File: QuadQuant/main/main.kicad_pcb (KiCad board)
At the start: 2 copper layers, 30.5 x 101.6 mm, 71 parts, among them J1 USB_B_Mini, J10 CV4, J11 Trig1, J12 Trig2, J13 Trig4, J14 Trig3, J2 Conn_02x05_Odd_Even, J3 OUT2, J4 OUT3, J5 OUT4, J6 OUT1, J7 CV1, J8 CV2, J9 CV3, Q1 MMBT3904, Q2 MMBT3904, Q3 MMBT3904, Q4 MMBT3904, U1 LM7805_TO220, U2 ATmega32U4-AU, U3 MCP4728, U4 TL074, Y1 Crystal16mhz

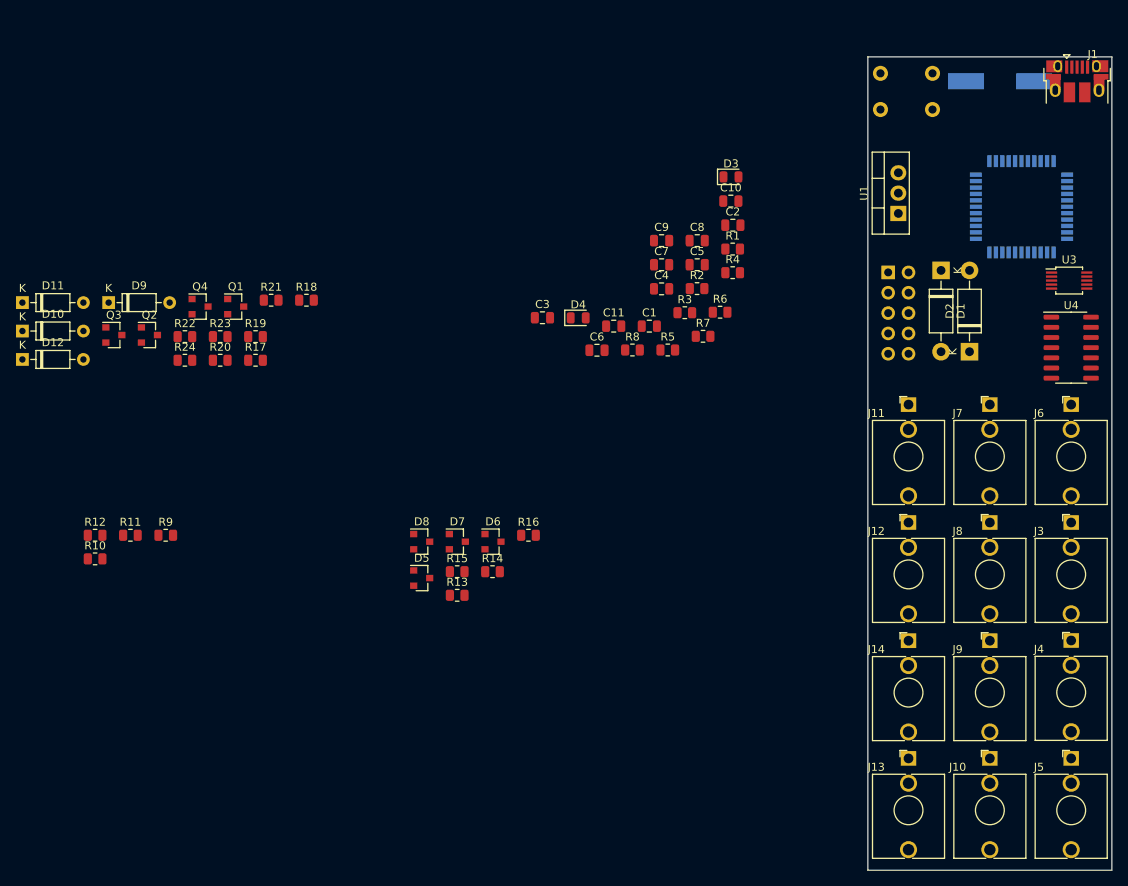
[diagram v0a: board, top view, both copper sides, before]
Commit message: Adding programming headers
Also starting in on a PCB layout. My smd work is so fugly right now.
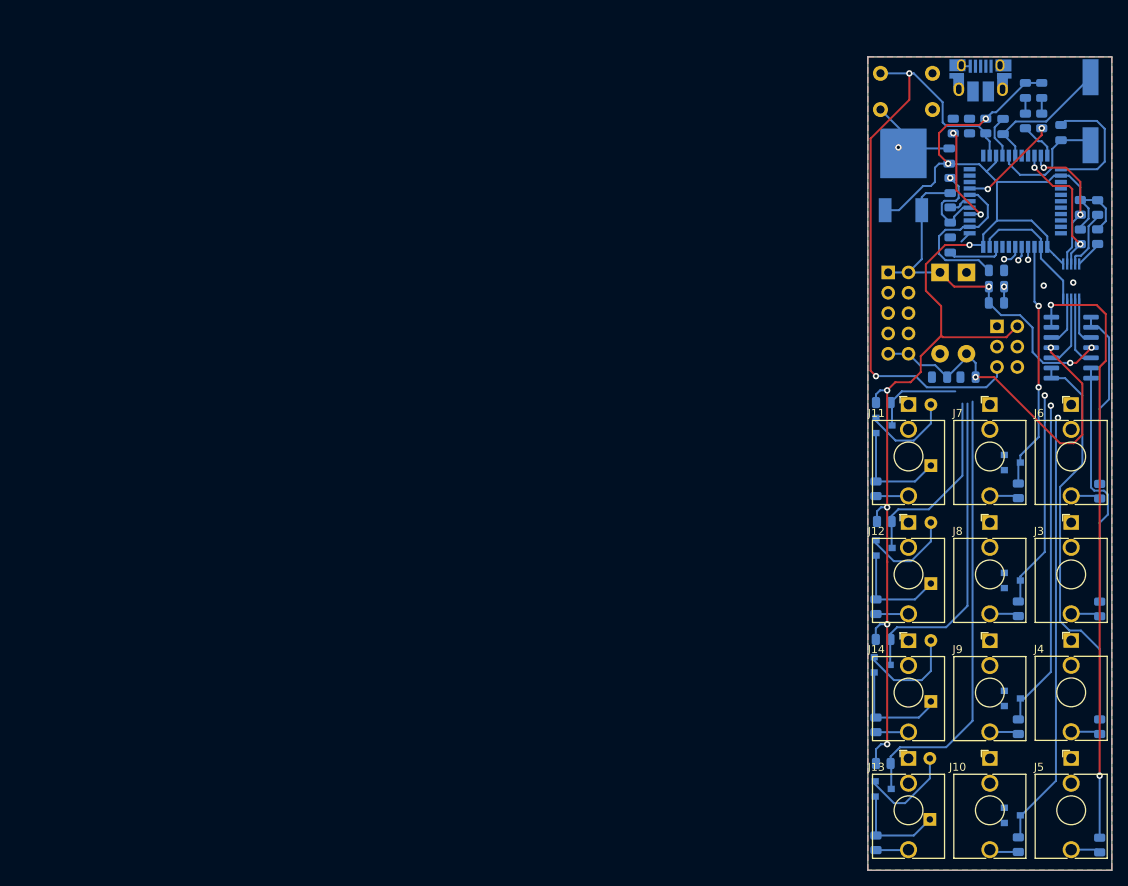
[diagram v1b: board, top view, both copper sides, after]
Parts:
- removed U1: LM7805_TO220, Package_TO_SOT_THT:TO-220-3_Vertical
- added IC1: MC7805CDTRKG, SamacSys_Parts:MJD1221G, B.Cu at (156.8, 68.5)
- added J15: Conn_02x03_Odd_Even, Connector_PinSocket_2.54mm:PinSocket_2x03_P2.54mm_Vertical, B.Cu at (168.5, 84.5)
- added R25: 1K, Resistor_SMD:R_0805_2012Metric, B.Cu at (172.1, 58.8)
- C1, C10, C11, C2, C3, C4, C5, C6, C7, C8, C9, D1, D10, D11, D12, D2, D3, D4, D5, D6, D7, D8, D9, J1, Q1, Q2, Q3, Q4, R1, R10, R11, R12, R13, R14, R15, R16, R17, R18, R19, R2, R20, R21, R22, R23, R24, R3, R4, R5, R6, R7, R8, R9, U3, U4: moved to B.Cu
- moved D11 130.4 mm to (160.1, 146.1), turned to 90 degrees
- moved R10 127.2 mm to (181.4, 134.5), turned to 90 degrees
- moved R11 127.1 mm to (181.4, 149.2), turned to 90 degrees
- moved R12 125.6 mm to (181.4, 105.1), turned to 90 degrees
- moved D12 121.3 mm to (160.3, 131.3), turned to 90 degrees
- moved D10 117.8 mm to (160.3, 116.6), turned to 90 degrees
- moved R9 117.0 mm to (181.4, 119.8), turned to 90 degrees
- moved Q3 111.6 mm to (154.3, 142.2)
- moved D9 104.7 mm to (160.3, 101.9), turned to 90 degrees
- moved R21 101.5 mm to (153.4, 149.0), turned to 270 degrees
- moved R22 99.0 mm to (153.4, 134.2), turned to 270 degrees
- moved R23 98.5 mm to (154.3, 139.1), turned to 180 degrees
- moved Q4 96.2 mm to (154.2, 126.7)
- moved Q2 95.5 mm to (154.4, 112.1)
- moved R24 93.9 mm to (154.3, 123.6), turned to 180 degrees
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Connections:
- net Net-(R3-Pad2) renamed RST
- C6 pad 1: GND -> +5V
- C6 pad 2: +5V -> GND
- J1 pad 4: Net-(J1-Pad4) -> (no net)
- U2 pad 1: Net-(U2-Pad1) -> Trigger3
- U2 pad 10: Net-(U2-Pad10) -> MOSI
- U2 pad 11: Net-(U2-Pad11) -> MISO
- U2 pad 12: Net-(U2-Pad12) -> (no net)
- U2 pad 18: Net-(U2-Pad18) -> (no net)
- U2 pad 19: Net-(U2-Pad19) -> (no net)
- U2 pad 22: Net-(D3-Pad1) -> Net-(R25-Pad2)
- U2 pad 25: Net-(U2-Pad25) -> (no net)
- U2 pad 26: Net-(U2-Pad26) -> (no net)
- U2 pad 27: Net-(U2-Pad27) -> Trigger4
- U2 pad 28: Net-(U2-Pad28) -> Trigger2
- U2 pad 29: Net-(U2-Pad29) -> Trigger1
- U2 pad 30: Net-(U2-Pad30) -> (no net)
- U2 pad 31: Net-(U2-Pad31) -> (no net)
- U2 pad 32: Net-(U2-Pad32) -> (no net)
- U2 pad 33: Net-(U2-Pad33) -> (no net)
- U2 pad 36: Net-(U2-Pad36) -> CVA
- U2 pad 37: Net-(U2-Pad37) -> CVB
- U2 pad 38: Net-(U2-Pad38) -> CVC
- U2 pad 39: Net-(U2-Pad39) -> CVD
- U2 pad 40: Net-(U2-Pad40) -> (no net)
- U2 pad 41: Net-(U2-Pad41) -> (no net)
- U2 pad 9: Net-(U2-Pad9) -> SCK
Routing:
- net +5V: track 0.00 -> 180.1 mm, vias 0 -> 7
- net GND: track 0.00 -> 111.6 mm, vias 0 -> 5
- net RST: track 0.00 -> 78.3 mm, vias 0 -> 2
- net Net-(R11-Pad2): track 0.00 -> 75.9 mm, vias 0 -> 2
- net CVD: track 0.00 -> 57.2 mm, vias 0 -> 2
- net Trigger4: track 0.00 -> 56.0 mm
- net Net-(R10-Pad2): track 0.00 -> 50.5 mm
- net +12V: track 0.00 -> 47.7 mm, vias 0 -> 3
- net -12V: track 0.00 -> 45.6 mm, vias 0 -> 2
- net CVC: track 0.00 -> 43.0 mm, vias 0 -> 2
- net Trigger3: track 0.00 -> 41.7 mm
- net Net-(R9-Pad2): track 0.00 -> 31.2 mm
- net CVA: track 0.00 -> 30.8 mm, vias 0 -> 2
- net CVB: track 0.00 -> 28.7 mm, vias 0 -> 2
- net Trigger2: track 0.00 -> 24.0 mm
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- added copper zone on B.Cu, net GND
- added copper zone on F.Cu, net GND

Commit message: Hmm. Feeling stuck
Saving progress so I can get back here if necessary
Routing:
- net Trigger4: track 56.0 -> 94.4 mm, vias 0 -> 2
- net Trigger3: track 41.7 -> 78.7 mm, vias 0 -> 2
- net Trigger1: track 11.6 -> 47.7 mm, vias 0 -> 2
- net Trigger2: track 24.0 -> 59.1 mm, vias 0 -> 2
- net CVD: track 57.2 -> 80.1 mm
- net CVC: track 43.0 -> 64.9 mm
- net vbus: track 20.7 -> 42.1 mm, vias 0 -> 1
- net CVB: track 28.7 -> 47.1 mm
- net Net-(R2-Pad1): track 0.00 -> 13.8 mm, vias 0 -> 2
- net Net-(R11-Pad2): track 75.9 -> 67.5 mm
- net +5V: track 180.1 -> 173.9 mm, vias 7 -> 8
- net +12V: track 47.7 -> 51.0 mm, vias 3 -> 1
- net GND: track 111.6 -> 113.4 mm, vias 5 -> 11
- net Net-(R1-Pad1): track 13.0 -> 13.9 mm

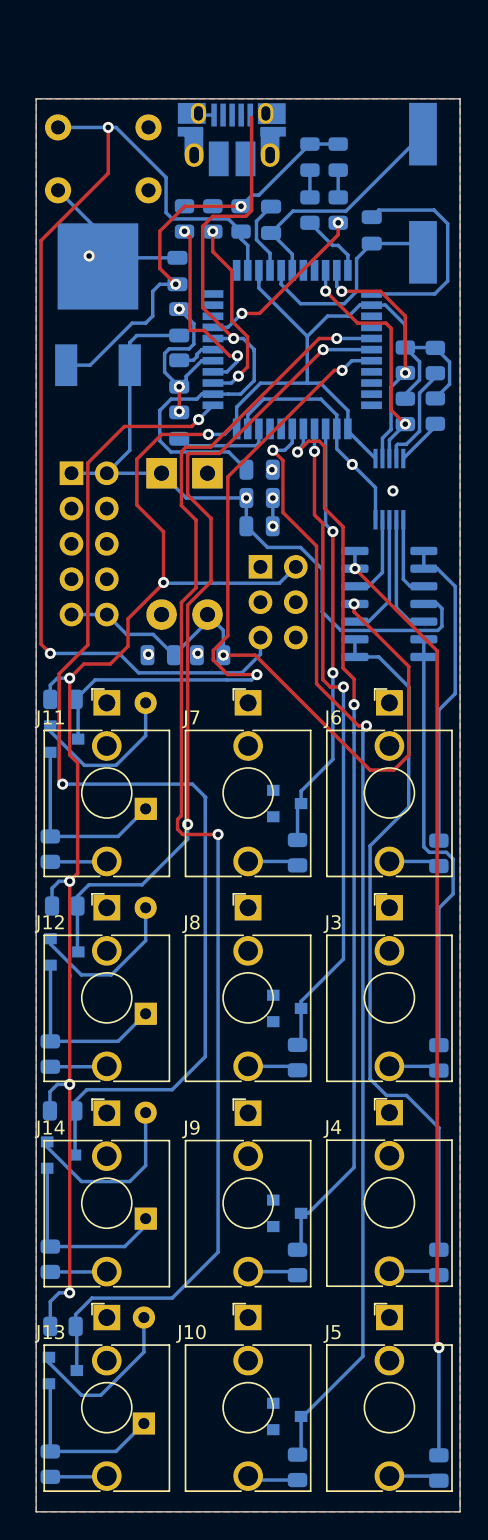
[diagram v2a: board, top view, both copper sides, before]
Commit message: quantizer first pass at routing
Much better with a hair more breathing room. Also I think I had the usb flipped backwards. Fixed.
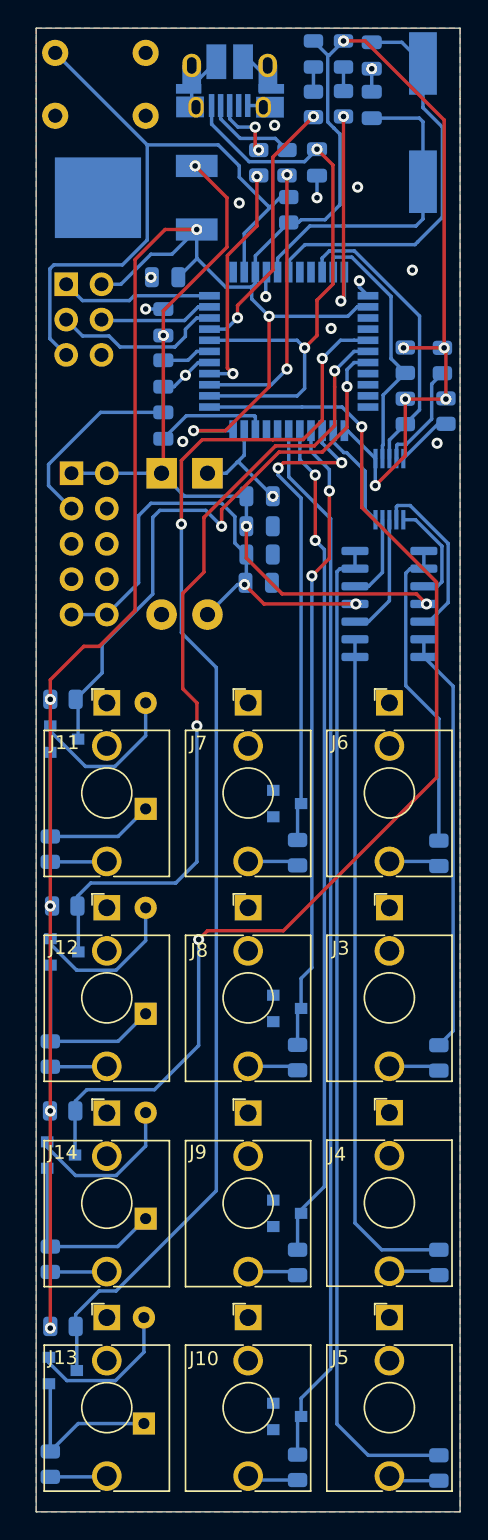
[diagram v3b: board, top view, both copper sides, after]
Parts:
- C11: value C_Small -> 100n
- moved J15 24.7 mm to (154.6, 64.1)
- moved C2 22.5 mm to (172.6, 55.4), turned to 90 degrees
- moved C3 13.9 mm to (176.5, 47.7), turned to 270 degrees
- moved IC1 11.9 mm to (162.4, 57.9), turned to 0 degrees
- moved C4 9.02 mm to (176.5, 51.2)
- moved C9 8.76 mm to (168.4, 85.6), turned to 0 degrees
- moved C11 8.06 mm to (168.5, 83.6), turned to 0 degrees
- moved R25 8.02 mm to (174.5, 51.2)
- moved R4 7.80 mm to (172.3, 51.2)
- moved D3 7.80 mm to (174.5, 47.6)
- moved D4 7.62 mm to (172.3, 47.6)
- moved R2 6.69 mm to (170.4, 55.4)
- moved R1 6.69 mm to (168.4, 55.4)
- moved RESET1 5.36 mm to (157.0, 49.8)
- moved Y1 5.08 mm to (180.2, 52.5)
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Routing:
- net RST: track 78.3 -> 49.0 mm, vias 2 -> 0
- net +5V: track 173.9 -> 199.1 mm, vias 8 -> 13
- net GND: track 113.4 -> 97.0 mm, vias 11 -> 15
- net SCK: track 0.00 -> 12.3 mm
- net Net-(C3-Pad1): track 17.2 -> 29.1 mm
- net MISO: track 0.00 -> 10.9 mm
- net Net-(R25-Pad2): track 4.79 -> 15.6 mm, vias 0 -> 2
- net -12V: track 45.6 -> 35.7 mm
- net MOSI: track 0.00 -> 8.20 mm
- net Net-(C4-Pad1): track 15.2 -> 23.4 mm
- net Net-(J1-Pad2): track 0.00 -> 6.66 mm
- net Net-(R4-Pad2): track 12.6 -> 19.1 mm
- net Net-(R2-Pad1): track 13.8 -> 20.0 mm
- net +12V: track 51.0 -> 57.0 mm, vias 1 -> 4
- net Trigger1: track 47.7 -> 42.5 mm
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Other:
- board size 30.5 x 101.6 mm -> 30.5 x 106.7 mm
- board text added: "-12V"
- board text added: "5v"
- board text added: "Gray Noise Audio"
- board text added: "gnd"
- board text added: "miso"
- board text added: "mosi"
- board text added: "quant v1"
- board text added: "rst"
- board text added: "sck"
